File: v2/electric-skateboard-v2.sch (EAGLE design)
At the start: 60 parts, among them J1 ZX62D-B-5P8, Q1 NTR4501N-D, Q2 NTR4501N-D, U1 SPX29300, U2 LDO, U3 MPU-9150, U5 STM32F4V

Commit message: In theory I could ship this layout but I'm ashamed of it. It's gross.
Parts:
- removed TP3, TP4: TPTP06R, testpad:TPTP06R
- CTS1: value 25MHz -> (none); device crystal:CRYSTALCTS406 -> adafruit:CRYSTALCTS406
- JP6: value (none) -> PRESSA
- JP7: value (none) -> PRESSB
- JP9: value (none) -> LCD
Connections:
- net N$1 renamed SDA2
- net N$10 renamed ESCB
- net N$12 renamed ESCA
- net N$7 renamed SCL2
- net CLKOUT: now also U5.PE1; no longer U5.PD9
- net GND: no longer TP3.TP, TP4.TP
- net INT: now also U5.PE0; no longer U5.PD8
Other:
- note removed: "CLKIN"
- note removed: "FSYNC"
- moved on the sheet: CTS1
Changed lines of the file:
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@@
 <part name="C22" library="SparkFun-Passives" deviceset="CAP" device="0402-CAP" value="100nF"/>
 <part name="DIG_GND28" library="SparkFun-Aesthetics" deviceset="GND" device="" value="GND"/>
-<part name="CTS1" library="crystal" deviceset="CRYSTAL" device="CTS406" value="25MHz"/>
 <part name="C16" library="SparkFun-Passives" deviceset="CAP" device="0402-CAP" value="15pF"/>
 <part name="C19" library="SparkFun-Passives" deviceset="CAP" device="0402-CAP" value="15pF"/>
@@
 <part name="P+6" library="SparkFun-Aesthetics" deviceset="3.3V" device=""/>
 <part name="P+5" library="SparkFun-Aesthetics" deviceset="3.3V" device=""/>
-<part name="TP3" library="testpad" deviceset="TP" device="TP06R" value="TPTP06R"/>
-<part name="TP4" library="testpad" deviceset="TP" device="TP06R" value="TPTP06R"/>
 <part name="Q1" library="max-viz" deviceset="NTR4501N-D" device="" value=""/>
 <part name="DIG_GND2" library="SparkFun-Aesthetics" deviceset="GND" device="" value="GND"/>
@@
 <part name="DIG_GND6" library="SparkFun-Aesthetics" deviceset="GND" device="" value="GND"/>
 <part name="DIG_GND7" library="SparkFun-Aesthetics" deviceset="GND" device="" value="GND"/>
-<part name="JP6" library="SparkFun-Connectors" deviceset="M04" device="LOCK_LONGPADS"/>
-<part name="JP7" library="SparkFun-Connectors" deviceset="M04" device="LOCK_LONGPADS"/>
+<part name="JP6" library="SparkFun-Connectors" deviceset="M04" device="LOCK_LONGPADS" value="PRESSA"/>
+<part name="JP7" library="SparkFun-Connectors" deviceset="M04" device="LOCK_LONGPADS" value="PRESSB"/>
 <part name="DIG_GND8" library="SparkFun-Aesthetics" deviceset="GND" device="" value="GND"/>
 <part name="DIG_GND10" library="SparkFun-Aesthetics" deviceset="GND" device="" value="GND"/>
@@
 <part name="DIG_GND15" library="SparkFun-Aesthetics" deviceset="GND" device="" value="GND"/>
 <part name="JP8" library="SparkFun-Connectors" deviceset="M03X2" device="FEMALE" value="FEMALE 2x3"/>
-<part name="JP9" library="SparkFun-Connectors" deviceset="M04" device="SCREW_LOCK"/>
+<part name="JP9" library="SparkFun-Connectors" deviceset="M04" device="SCREW_LOCK" value="LCD"/>
 <part name="P5V11" library="max-viz" deviceset="5V" device=""/>
 <part name="DIG_GND14" library="SparkFun-Aesthetics" deviceset="GND" device="" value="GND"/>
+<part name="CTS1" library="adafruit" deviceset="CRYSTAL" device="CTS406"/>
 </parts>
 <sheets>
@@
 LSB of 7 bit address to zero.
 Default Address = 0x68</text>
-<text x="0" y="76.962" size="1.778" layer="97">FSYNC</text>
-<text x="14.224" y="77.216" size="1.778" layer="97">CLKIN</text>
 <text x="75.184" y="48.26" size="1.778" layer="97">MPU9150 is set for Primary I2C Mode
 E_SCL and E_SDA are not connected.</text>
@@
 <instance part="C22" gate="G$1" x="322.58" y="215.9" rot="MR180"/>
 <instance part="DIG_GND28" gate="1" x="322.58" y="205.74" rot="MR0"/>
-<instance part="CTS1" gate="G$1" x="322.58" y="187.96"/>
 <instance part="C16" gate="G$1" x="317.5" y="180.34" rot="R180"/>
 <instance part="C19" gate="G$1" x="335.28" y="180.34" rot="R180"/>
@@
 <instance part="P+6" gate="G$1" x="25.4" y="99.06"/>
 <instance part="P+5" gate="G$1" x="106.68" y="104.14"/>
-<instance part="TP3" gate="G$1" x="5.08" y="73.66"/>
-<instance part="TP4" gate="G$1" x="15.24" y="73.66"/>
 <instance part="Q1" gate="G$1" x="421.64" y="170.18"/>
 <instance part="DIG_GND2" gate="1" x="421.64" y="162.56"/>
@@
 <instance part="DIG_GND10" gate="1" x="406.4" y="60.96"/>
 <instance part="P5V9" gate="G$1" x="365.76" y="76.2"/>
-<instance part="P5V10" gate="G$1" x="406.4" y="76.2"/>
-<instance part="P+2" gate="G$1" x="396.24" y="76.2"/>
+<instance part="P5V10" gate="G$1" x="403.86" y="76.2"/>
+<instance part="P+2" gate="G$1" x="393.7" y="76.2"/>
 <instance part="P+8" gate="G$1" x="353.06" y="76.2"/>
 <instance part="J1" gate="G$1" x="50.8" y="142.24" smashed="yes">
@@
 <instance part="P5V11" gate="G$1" x="172.72" y="137.16"/>
 <instance part="DIG_GND14" gate="1" x="172.72" y="121.92" rot="MR0"/>
+<instance part="CTS1" gate="G$1" x="325.12" y="187.96"/>
 </instances>
 <busses>
@@
 <segment>
 <pinref part="JP7" gate="G$1" pin="2"/>
-<wire x1="408.94" y1="71.12" x2="396.24" y2="71.12" width="0.1524" layer="91"/>
-<wire x1="396.24" y1="71.12" x2="396.24" y2="76.2" width="0.1524" layer="91"/>
+<wire x1="408.94" y1="71.12" x2="393.7" y2="71.12" width="0.1524" layer="91"/>
+<wire x1="393.7" y1="71.12" x2="393.7" y2="76.2" width="0.1524" layer="91"/>
 <pinref part="P+2" gate="G$1" pin="3.3V"/>
 </segment>
@@
 <wire x1="53.34" y1="66.04" x2="15.24" y2="66.04" width="0.1524" layer="91"/>
 <wire x1="15.24" y1="66.04" x2="15.24" y2="53.34" width="0.1524" layer="91"/>
-<pinref part="TP4" gate="G$1" pin="TP"/>
-<wire x1="15.24" y1="66.04" x2="15.24" y2="71.12" width="0.1524" layer="91"/>
-<junction x="15.24" y="66.04"/>
 </segment>
 <segment>
@@
 <wire x1="53.34" y1="68.58" x2="5.08" y2="68.58" width="0.1524" layer="91"/>
 <wire x1="5.08" y1="68.58" x2="5.08" y2="53.34" width="0.1524" layer="91"/>
-<pinref part="TP3" gate="G$1" pin="TP"/>
-<wire x1="5.08" y1="68.58" x2="5.08" y2="71.12" width="0.1524" layer="91"/>
-<junction x="5.08" y="68.58"/>
 </segment>
 <segment>
@@
 <pinref part="C16" gate="G$1" pin="2"/>
 <wire x1="304.8" y1="187.96" x2="317.5" y2="187.96" width="0.15" layer="91"/>
-<pinref part="CTS1" gate="G$1" pin="1"/>
 <wire x1="317.5" y1="187.96" x2="317.5" y2="182.88" width="0.15" layer="91"/>
-<wire x1="320.04" y1="187.96" x2="317.5" y2="187.96" width="0.15" layer="91"/>
+<wire x1="322.58" y1="187.96" x2="317.5" y2="187.96" width="0.15" layer="91"/>
 <wire x1="292.1" y1="172.72" x2="304.8" y2="172.72" width="0.15" layer="91"/>
 <wire x1="304.8" y1="172.72" x2="304.8" y2="187.96" width="0.15" layer="91"/>
 <junction x="317.5" y="187.96"/>
 <pinref part="U5" gate="G$1" pin="PH1"/>
+<pinref part="CTS1" gate="G$1" pin="1"/>
 </segment>
 </net>
 <net name="OSC_IN1" class="0">
 <segment>
-<pinref part="CTS1" gate="G$1" pin="2"/>
-<wire x1="325.12" y1="187.96" x2="335.28" y2="187.96" width="0.15" layer="91"/>
+<wire x1="327.66" y1="187.96" x2="335.28" y2="187.96" width="0.15" layer="91"/>
 <pinref part="C19" gate="G$1" pin="2"/>
 <wire x1="335.28" y1="182.88" x2="335.28" y2="187.96" width="0.15" layer="91"/>
@@
 <junction x="335.28" y="187.96"/>
 <pinref part="U5" gate="G$1" pin="PH0"/>
+<pinref part="CTS1" gate="G$1" pin="2"/>
 </segment>
 </net>
@@
 </segment>
 <segment>
-<wire x1="406.4" y1="76.2" x2="406.4" y2="73.66" width="0.1524" layer="91"/>
+<wire x1="403.86" y1="76.2" x2="403.86" y2="73.66" width="0.1524" layer="91"/>
 <pinref part="JP7" gate="G$1" pin="1"/>
-<wire x1="406.4" y1="73.66" x2="408.94" y2="73.66" width="0.1524" layer="91"/>
+<wire x1="403.86" y1="73.66" x2="408.94" y2="73.66" width="0.1524" layer="91"/>
 <pinref part="P5V10" gate="G$1" pin="5V"/>
 </segment>
@@
 <pinref part="U5" gate="G$1" pin="PB9"/>
 <wire x1="116.84" y1="101.6" x2="200.66" y2="101.6" width="0.1524" layer="91"/>
-<label x="190.5" y="101.6" size="1.778" layer="95"/>
+<label x="185.42" y="101.6" size="1.778" layer="95"/>
 </segment>
 </net>
@@
 <pinref part="U5" gate="G$1" pin="PB8"/>
 <wire x1="200.66" y1="99.06" x2="119.38" y2="99.06" width="0.1524" layer="91"/>
-<label x="190.5" y="99.06" size="1.778" layer="95"/>
+<label x="185.42" y="99.06" size="1.778" layer="95"/>
 </segment>
 </net>
@@
 <pinref part="U3" gate="G$1" pin="INT"/>
 <label x="91.44" y="76.2" size="1.778" layer="95"/>
-<wire x1="88.9" y1="76.2" x2="190.5" y2="76.2" width="0.1524" layer="91"/>
-<wire x1="190.5" y1="76.2" x2="190.5" y2="63.5" width="0.1524" layer="91"/>
-<pinref part="U5" gate="G$1" pin="PD8"/>
-<wire x1="190.5" y1="63.5" x2="200.66" y2="63.5" width="0.1524" layer="91"/>
+<wire x1="88.9" y1="76.2" x2="180.34" y2="76.2" width="0.1524" layer="91"/>
+<wire x1="180.34" y1="76.2" x2="180.34" y2="93.98" width="0.1524" layer="91"/>
+<wire x1="180.34" y1="93.98" x2="200.66" y2="93.98" width="0.1524" layer="91"/>
+<pinref part="U5" gate="G$1" pin="PE0"/>
+<label x="185.42" y="93.98" size="1.778" layer="95"/>
 </segment>
 </net>
@@
 <segment>
 <pinref part="U3" gate="G$1" pin="CLKOUT"/>
-<wire x1="88.9" y1="73.66" x2="187.96" y2="73.66" width="0.1524" layer="91"/>
+<wire x1="88.9" y1="73.66" x2="182.88" y2="73.66" width="0.1524" layer="91"/>
 <label x="91.44" y="73.66" size="1.778" layer="95"/>
-<wire x1="187.96" y1="73.66" x2="187.96" y2="60.96" width="0.1524" layer="91"/>
-<pinref part="U5" gate="G$1" pin="PD9"/>
-<wire x1="200.66" y1="60.96" x2="187.96" y2="60.96" width="0.1524" layer="91"/>
+<wire x1="182.88" y1="73.66" x2="182.88" y2="91.44" width="0.1524" layer="91"/>
+<wire x1="182.88" y1="91.44" x2="200.66" y2="91.44" width="0.1524" layer="91"/>
+<pinref part="U5" gate="G$1" pin="PE1"/>
+<label x="185.42" y="91.44" size="1.778" layer="95"/>
 </segment>
 </net>
@@
 </segment>
 </net>
-<net name="N$10" class="0">
+<net name="ESCB" class="0">
 <segment>
 <pinref part="JP5" gate="G$1" pin="1"/>
@@
 </segment>
 </net>
-<net name="N$12" class="0">
+<net name="ESCA" class="0">
 <segment>
 <pinref part="JP4" gate="G$1" pin="1"/>
@@
 </segment>
 </net>
-<net name="N$1" class="0">
+<net name="SDA2" class="0">
 <segment>
 <pinref part="U5" gate="G$1" pin="PB11"/>
@@
 <wire x1="185.42" y1="132.08" x2="185.42" y2="137.16" width="0.1524" layer="91" style="longdash"/>
 <wire x1="185.42" y1="137.16" x2="200.66" y2="137.16" width="0.1524" layer="91"/>
-</segment>
-</net>
-<net name="N$7" class="0">
+<label x="172.72" y="132.08" size="1.778" layer="95"/>
+</segment>
+</net>
+<net name="SCL2" class="0">
 <segment>
 <pinref part="U5" gate="G$1" pin="PB10"/>
@@
 <wire x1="187.96" y1="129.54" x2="185.42" y2="129.54" width="0.1524" layer="91"/>
 <wire x1="185.42" y1="129.54" x2="170.18" y2="129.54" width="0.1524" layer="91"/>
-</segment>
-</net>
+<label x="172.72" y="129.54" size="1.778" layer="95"/>
+</segment>
+</net>

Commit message: Needs final review but otherwise layout is done.
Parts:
- removed JP1: BATT, SparkFun-Connectors:M025MM
- added BATTERY_IN: BATT, SparkFun-Connectors:M025MM
- C1, C4: device SparkFun-Passives:CAP0603-CAP -> max-viz:CAP-1210
- C14, C15: device SparkFun-Passives:CAP0402-CAP -> max-viz:CAP-0805
- C16, C17, C18, C19, C2, C20, C21, C22, C23, C24, C5, C6, C7, C8, C9: device SparkFun-Passives:CAP0402-CAP -> max-viz:CAP-0402
- C3: device SparkFun-Passives:CAP0603-CAP -> max-viz:CAP-0402
- ESCA: value ESCA -> (none)
- ESCB: value ESCB -> (none)
- HALLA: value HALLA -> (none)
- HALLB: value HALLB -> (none)
- LCD: value LCD -> (none)
- LED1, LED2, LED6: device led:LEDCHIPLED_0603 -> max-viz:BG1111C
- PRESSA: value PRESSA -> (none)
- PRESSB: value PRESSB -> (none)
- R1, R11, R2: device SparkFun-Passives:RESISTOR0603-RES -> max-viz:RES-0402
- R10, R13, R15, R17, R3, R4, R5, R6, R9: device SparkFun-Passives:RESISTOR0402-RES -> max-viz:RES-0402
- R12, R14: device max-viz:RES-0805 -> max-viz:RES-0402
- renumbered JP2 to HALLA, JP3 to HALLB, JP4 to ESCA, JP5 to ESCB, JP6 to PRESSA, JP7 to PRESSB, JP9 to LCD
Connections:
- net GND: now also BATTERY_IN.2; no longer JP1.1
- net VIN: now also BATTERY_IN.1; no longer JP1.2
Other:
- moved on the sheet: C1, C14, C15, C16, C19, C2, C4, C5, C6, C7, C8, LED1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

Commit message: Shipping it.
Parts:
- removed R1: 240, max-viz:RES-0402
- removed R2: 390, max-viz:RES-0402
- removed U2: LDO, SparkFun-PowerIC:V_REG_317SMD
- added U4: AAT3221IGV-3.3-T1, SparkFun-DigitalIC:INVERTER_SOT23-5
- C3: device max-viz:CAP-0402 -> max-viz:CAP-1210
- C5, C8: value 0.1uF -> 100nF
- C6: value 2.2nF -> 100nF
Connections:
- removed net N$21: R1.1, R2.2, U2.ADJ
- net 3.3V: now also U4.OUT; no longer R1.2, U2.OUT
- net 5V: now also U4.EN, U4.IN; no longer U2.IN
- net GND: now also CTS1.GND, U4.GND; no longer R2.1
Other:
- moved on the sheet: C19, C6, C8

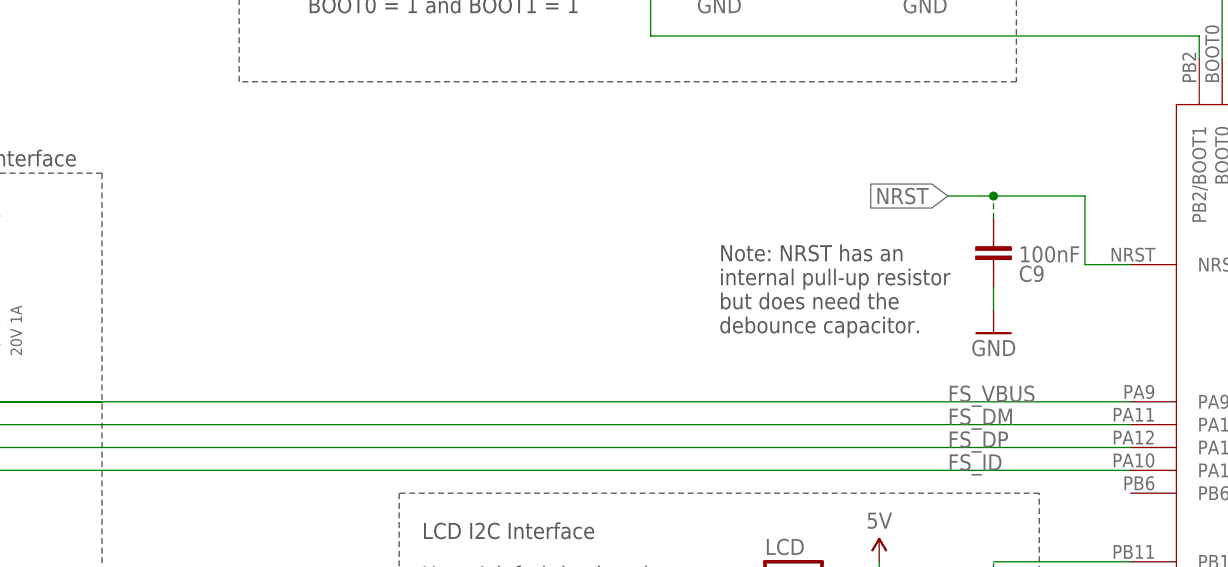
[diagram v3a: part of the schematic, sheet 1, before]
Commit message: Added button. Changed LDO.
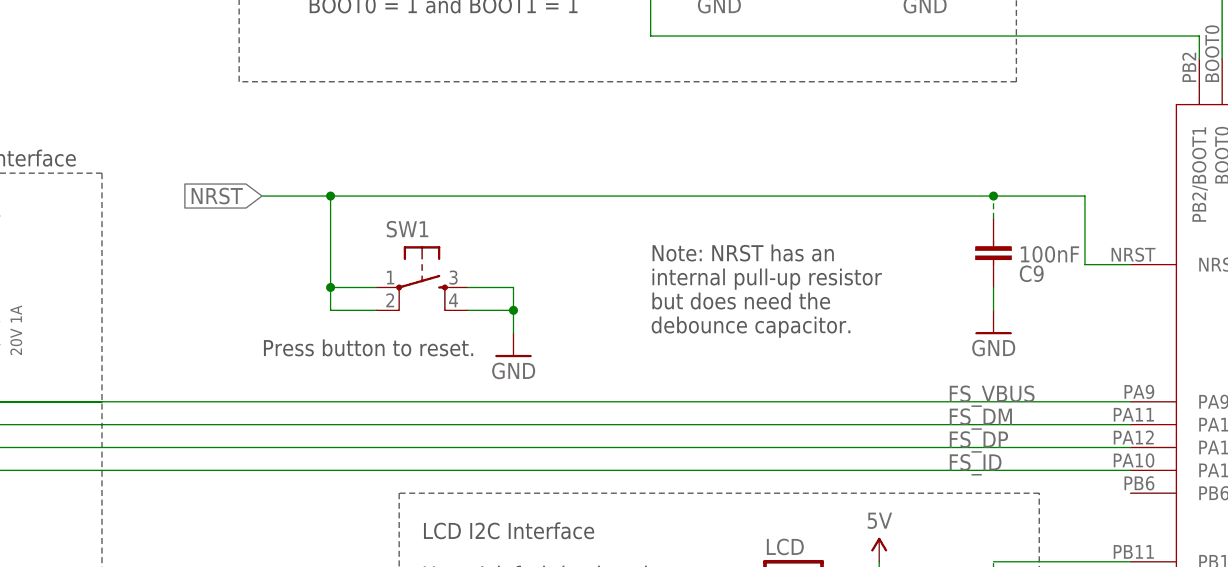
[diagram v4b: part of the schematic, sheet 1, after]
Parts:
- added SW1: TACTILE-SWITCH-PTH, GeekAmmo:TACTILE-SWITCH-PTH
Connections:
- net GND: now also SW1.3, SW1.4
- net NRST: now also SW1.1, SW1.2
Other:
- note added: "Press button to reset."
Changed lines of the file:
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@@
 <part name="DIG_GND16" library="SparkFun-Aesthetics" deviceset="GND" device="" value="GND"/>
 <part name="U4" library="SparkFun-DigitalIC" deviceset="INVERTER" device="_SOT23-5" value="AAT3221IGV-3.3-T1"/>
+<part name="SW1" library="GeekAmmo" deviceset="TACTILE-SWITCH" device="-PTH" value=""/>
+<part name="DIG_GND17" library="SparkFun-Aesthetics" deviceset="GND" device="" value="GND"/>
 </parts>
 <sheets>
@@
 <wire x1="134.62" y1="20.32" x2="-5.08" y2="20.32" width="0.1524" layer="97" style="shortdash"/>
 <text x="70.104" y="113.03" size="1.778" layer="97">Inertial Measurement: Compass, Gyro, and Accelerometer</text>
-<text x="154.94" y="162.56" size="1.778" layer="97">Note: NRST has an
+<text x="147.32" y="162.56" size="1.778" layer="97">Note: NRST has an
 internal pull-up resistor
 but does need the
@@
 <wire x1="195.58" y1="55.88" x2="144.78" y2="55.88" width="0.1524" layer="97" style="shortdash"/>
 <text x="146.304" y="57.15" size="1.778" layer="97">JTAG Programming</text>
+<text x="104.14" y="160.02" size="1.778" layer="97">Press button to reset.</text>
 </plain>
 <instances>
@@
 <instance part="CTS1" gate="G$1" x="325.12" y="187.96"/>
 <instance part="DIG_GND16" gate="1" x="325.12" y="180.34"/>
+<instance part="SW1" gate="G$1" x="121.92" y="167.64"/>
+<instance part="DIG_GND17" gate="1" x="132.08" y="160.02" rot="MR0"/>
 </instances>
 <busses>
@@
 <pinref part="DIG_GND16" gate="1" pin="GND"/>
 </segment>
+<segment>
+<pinref part="SW1" gate="G$1" pin="4"/>
+<wire x1="127" y1="165.1" x2="132.08" y2="165.1" width="0.1524" layer="91"/>
+<wire x1="132.08" y1="165.1" x2="132.08" y2="162.56" width="0.1524" layer="91"/>
+<pinref part="SW1" gate="G$1" pin="3"/>
+<wire x1="127" y1="167.64" x2="132.08" y2="167.64" width="0.1524" layer="91"/>
+<wire x1="132.08" y1="167.64" x2="132.08" y2="165.1" width="0.1524" layer="91"/>
+<junction x="132.08" y="165.1"/>
+<pinref part="DIG_GND17" gate="1" pin="GND"/>
+</segment>
 </net>
 <net name="FS_DP" class="0">
@@
 </segment>
 <segment>
-<label x="180.34" y="177.8" size="1.778" layer="95" rot="R180" xref="yes"/>
+<label x="104.14" y="177.8" size="1.778" layer="95" rot="R180" xref="yes"/>
 <pinref part="U5" gate="G$1" pin="NRST"/>
-<wire x1="180.34" y1="177.8" x2="185.42" y2="177.8" width="0.15" layer="91"/>
+<wire x1="104.14" y1="177.8" x2="111.76" y2="177.8" width="0.15" layer="91"/>
 <pinref part="C9" gate="G$1" pin="2"/>
+<wire x1="111.76" y1="177.8" x2="185.42" y2="177.8" width="0.15" layer="91"/>
 <wire x1="185.42" y1="177.8" x2="195.58" y2="177.8" width="0.15" layer="91"/>
 <wire x1="195.58" y1="177.8" x2="195.58" y2="170.18" width="0.15" layer="91"/>
@@
 <wire x1="185.42" y1="175.26" x2="185.42" y2="177.8" width="0.1524" layer="91" style="longdash"/>
 <junction x="185.42" y="177.8"/>
-</segment>
-</net>
+<pinref part="SW1" gate="G$1" pin="1"/>
+<wire x1="116.84" y1="167.64" x2="111.76" y2="167.64" width="0.1524" layer="91"/>
+<wire x1="111.76" y1="167.64" x2="111.76" y2="177.8" width="0.1524" layer="91"/>
+<junction x="111.76" y="177.8"/>
+<pinref part="SW1" gate="G$1" pin="2"/>
+<wire x1="116.84" y1="165.1" x2="111.76" y2="165.1" width="0.1524" layer="91"/>
+<wire x1="111.76" y1="165.1" x2="111.76" y2="167.64" width="0.1524" layer="91"/>
+<junction x="111.76" y="167.64"/>
+</segment>
+</net>
